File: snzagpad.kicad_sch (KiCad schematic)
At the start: 79 parts, among them J1 USB_C, J3 SWD, SW0 Boot, SW1 ?, SW10 ?, SW11 ?, SW12 ?, SW13 ?, SW14 ?, SW15 ?, SW16 ?, SW17 ?, SW18 ?, SW19 ?, SW2 ?, SW20 ?, SW21 ?, SW22 ?, SW23 ?, SW3 ?, SW4 ?, SW5 ?, SW6 ?, SW7 ?, SW8 ?, SW9 ?, U1 RP2040, U2 SRV05-4, U3 XC6206, U4 W25Q128JVS, Y1 12MHz

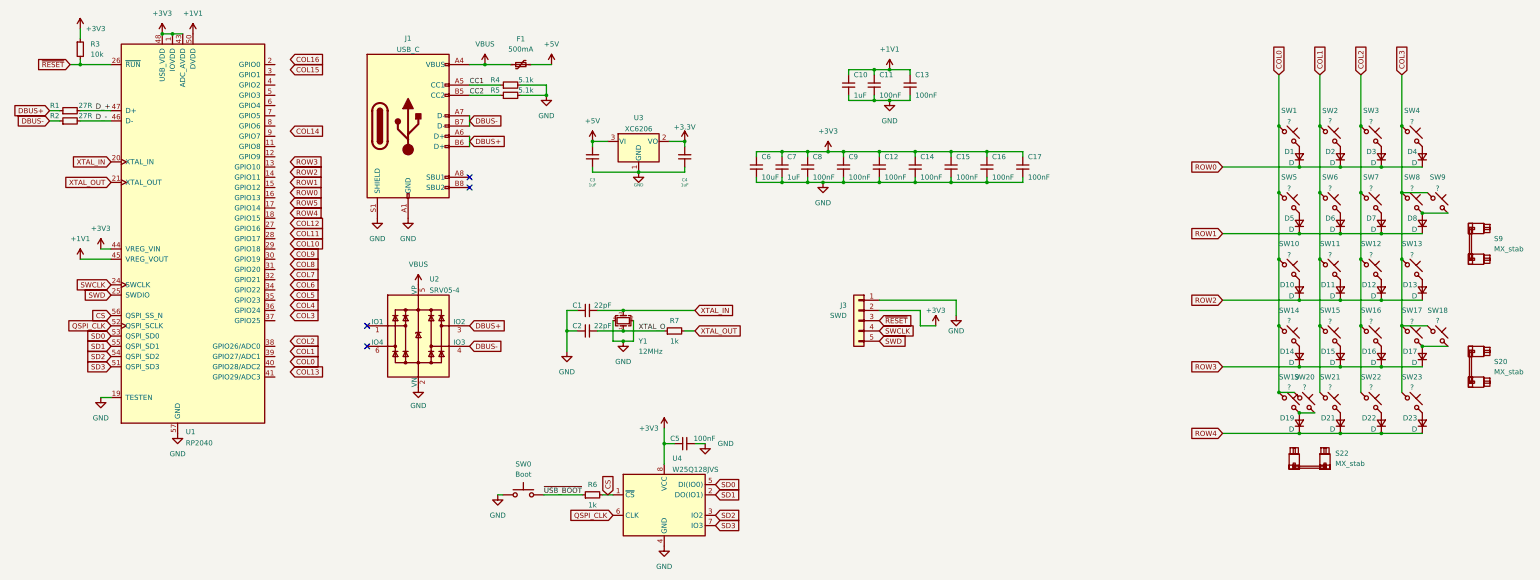
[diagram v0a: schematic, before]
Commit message: Updated outline, added mounts, preliminary routing
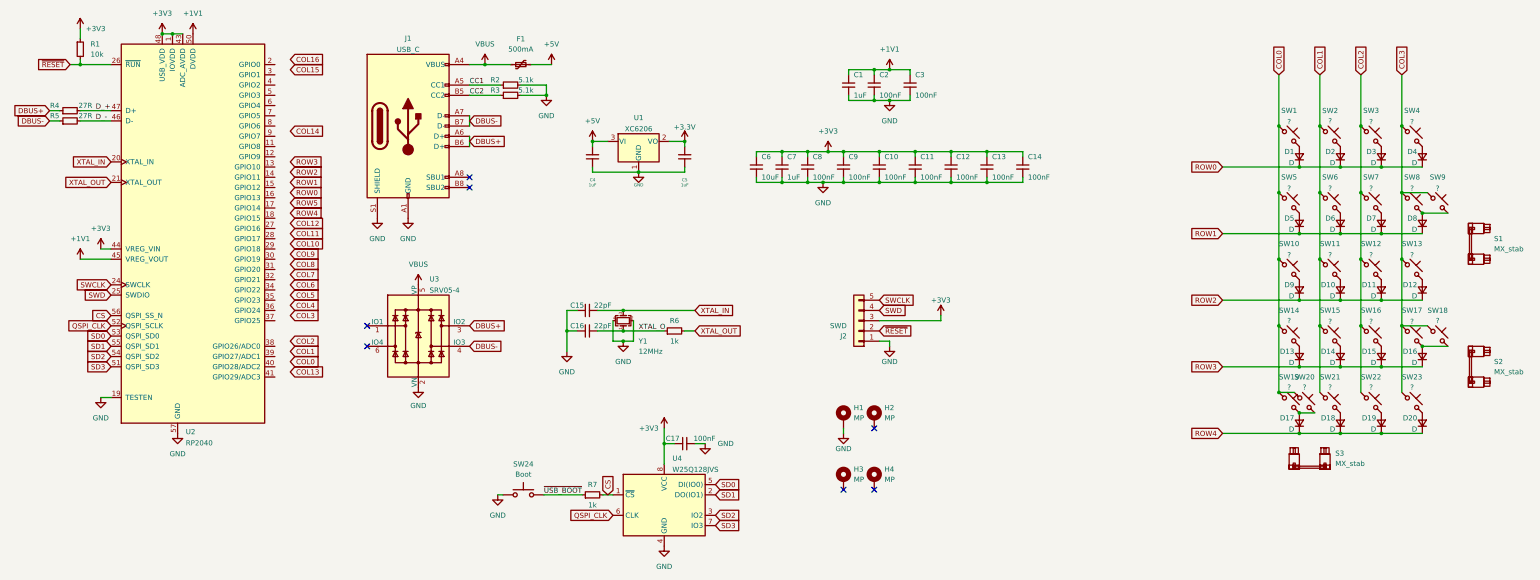
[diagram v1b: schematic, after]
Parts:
- added H1, H2, H3, H4: MP, MountingHole:MountingHole_2.2mm_M2_Pad, symbol Mechanical:MountingHole_Pad
- renumbered C10 to C1, C12 to C10, C14 to C11, C15 to C12, C16 to C13, C17 to C14, C1 to C15, C2 to C16, C5 to C17, C11 to C2, C13 to C3, C3 to C4, C4 to C5, D11 to D10, D12 to D11, D13 to D12, D14 to D13, D15 to D14, D16 to D15, D17 to D16, D19 to D17, D21 to D18, D22 to D19, D23 to D20, D10 to D9, J3 to J2, R3 to R1, R4 to R2, R5 to R3, R1 to R4, R2 to R5, R7 to R6, R6 to R7, S9 to S1, S20 to S2, S22 to S3, SW0 to SW24, U3 to U1, U1 to U2, U2 to U3
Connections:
- net +3V3: now also J2.3 (Pin_3); no longer J2.2 (Pin_2)
- net GND: now also H1.1
- net SWCLK: now also J2.5 (Pin_5); no longer J2.4 (Pin_4)
- net SWD: now also J2.4 (Pin_4); no longer J2.5 (Pin_5)
- net ~{RESET}: now also J2.2 (Pin_2); no longer J2.3 (Pin_3)
- no-connect marks 4 -> 7
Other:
- moved on the sheet: J2

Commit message: Edited cutout, mounts, USB position, routing
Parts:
- H1, H2, H3, H4: footprint MountingHole:MountingHole_2.2mm_M2_Pad -> MountingHole:MountingHole_2.2mm_M2_ISO14580_Pad
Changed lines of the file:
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@@
       (effects (font (size 1.27 1.27)) (justify left))
     )
-    (property "Footprint" "MountingHole:MountingHole_2.2mm_M2_Pad" (id 2) (at 234.95 134.62 0)
+    (property "Footprint" "MountingHole:MountingHole_2.2mm_M2_ISO14580_Pad" (id 2) (at 234.95 134.62 0)
       (effects (font (size 1.27 1.27)) hide)
     )
@@
       (effects (font (size 1.27 1.27)) (justify left))
     )
-    (property "Footprint" "MountingHole:MountingHole_2.2mm_M2_Pad" (id 2) (at 227.33 134.62 0)
+    (property "Footprint" "MountingHole:MountingHole_2.2mm_M2_ISO14580_Pad" (id 2) (at 227.33 134.62 0)
       (effects (font (size 1.27 1.27)) hide)
     )
@@
       (effects (font (size 1.27 1.27)) (justify left))
     )
-    (property "Footprint" "MountingHole:MountingHole_2.2mm_M2_Pad" (id 2) (at 227.33 119.38 0)
+    (property "Footprint" "MountingHole:MountingHole_2.2mm_M2_ISO14580_Pad" (id 2) (at 227.33 119.38 0)
       (effects (font (size 1.27 1.27)) hide)
     )
@@
       (effects (font (size 1.27 1.27)) (justify left))
     )
-    (property "Footprint" "MountingHole:MountingHole_2.2mm_M2_Pad" (id 2) (at 234.95 119.38 0)
+    (property "Footprint" "MountingHole:MountingHole_2.2mm_M2_ISO14580_Pad" (id 2) (at 234.95 119.38 0)
       (effects (font (size 1.27 1.27)) hide)
     )
@@
     )
     (path "/92ea1021-2dae-4d4a-b211-86ccee3ba4ed"
-      (reference "H1") (unit 1) (value "MP") (footprint "MountingHole:MountingHole_2.2mm_M2_Pad")
+      (reference "H1") (unit 1) (value "MP") (footprint "MountingHole:MountingHole_2.2mm_M2_ISO14580_Pad")
     )
     (path "/d755a3d1-521d-4d0c-aa97-92b99354f491"
-      (reference "H2") (unit 1) (value "MP") (footprint "MountingHole:MountingHole_2.2mm_M2_Pad")
+      (reference "H2") (unit 1) (value "MP") (footprint "MountingHole:MountingHole_2.2mm_M2_ISO14580_Pad")
     )
     (path "/5e972ae4-6f53-4eb5-97ac-b15ba7b7e923"
-      (reference "H3") (unit 1) (value "MP") (footprint "MountingHole:MountingHole_2.2mm_M2_Pad")
+      (reference "H3") (unit 1) (value "MP") (footprint "MountingHole:MountingHole_2.2mm_M2_ISO14580_Pad")
     )
     (path "/1aab2a5d-e09c-4385-855d-bfb45a77c796"
-      (reference "H4") (unit 1) (value "MP") (footprint "MountingHole:MountingHole_2.2mm_M2_Pad")
+      (reference "H4") (unit 1) (value "MP") (footprint "MountingHole:MountingHole_2.2mm_M2_ISO14580_Pad")
     )
     (path "/57dbda62-d28b-4d83-a763-2f2823178cf5"

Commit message: Completed mostly, rounded traces, connected everything
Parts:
- H1, H2, H3, H4, S1, S2, S3: now left out of the parts list
- J1: LCSC (none) -> C2982555
- SW1, SW10, SW11, SW12, SW13, SW14, SW15, SW16, SW17, SW18, SW19, SW2, SW20, SW21, SW22, SW23, SW3, SW4, SW5, SW6, SW7, SW8, SW9: LCSC (none) -> C2803348
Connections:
- net COL0: now also SW19.2, SW20.2, U2.8 (GPIO6); no longer SW19.1, SW20.1
- net COL1: now also U2.7 (GPIO5)
- net COL2: now also U2.6 (GPIO4)
- net COL3: now also U2.5 (GPIO3)
- net ROW0: now also U2.35 (GPIO23)
- net ROW1: now also U2.34 (GPIO22)
- net ROW2: now also U2.4 (GPIO2)
- net ROW3: now also U2.3 (GPIO1)
- net ROW4: now also U2.2 (GPIO0)
- new net: D17.2 (A), SW19.1, SW20.1
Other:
- moved on the sheet: SW19, SW20

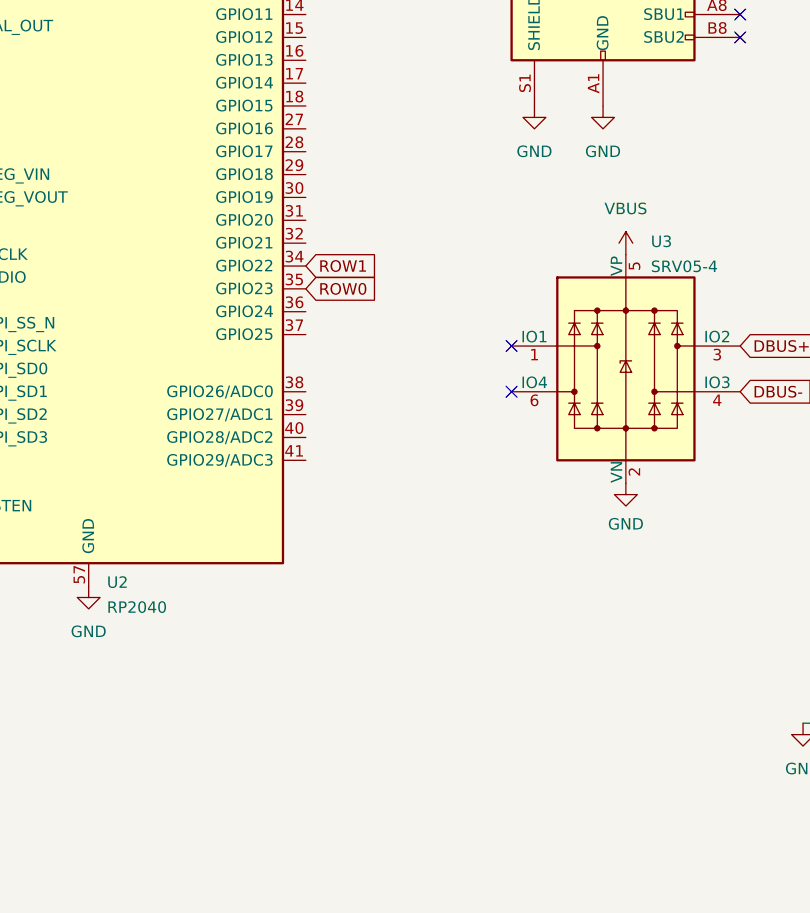
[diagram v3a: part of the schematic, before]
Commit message: Added GPIO breakout
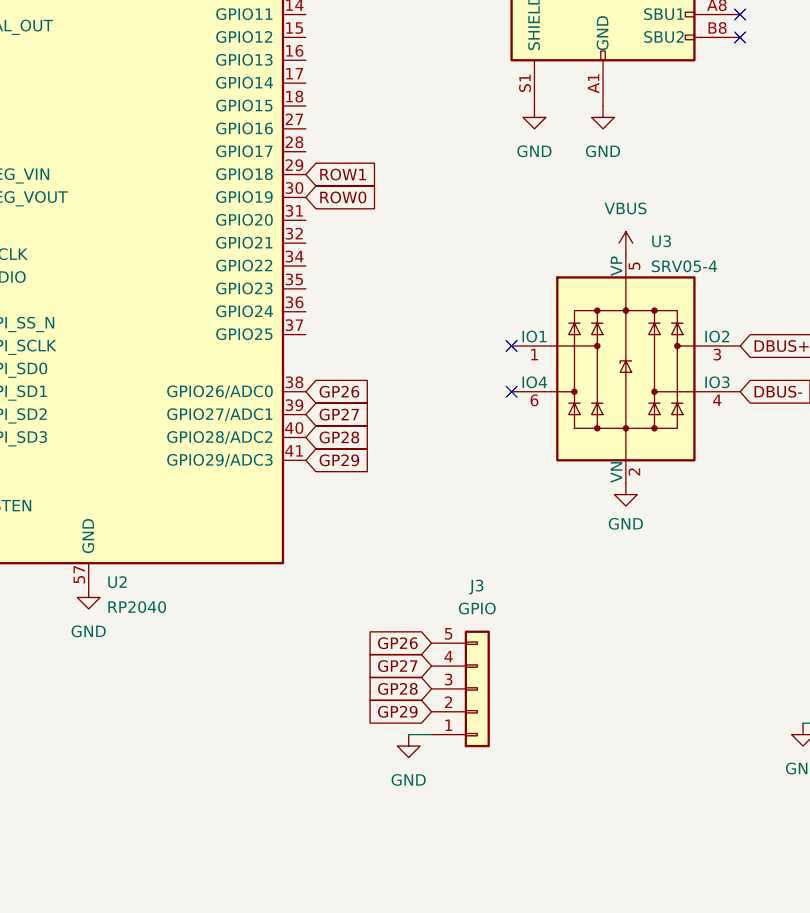
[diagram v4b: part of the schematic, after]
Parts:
- added J3: GPIO, Connector_PinHeader_1.00mm:PinHeader_1x05_P1.00mm_Vertical, symbol Connector_Generic:Conn_01x05
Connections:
- net GND: now also J3.1 (Pin_1)
- net ROW0: now also U2.30 (GPIO19); no longer U2.35 (GPIO23)
- net ROW1: now also U2.29 (GPIO18); no longer U2.34 (GPIO22)
- net GP26: now reaches U2.38 (GPIO26/ADC0)
- net GP26: now also J3.5 (Pin_5)
- net GP27: now reaches U2.39 (GPIO27/ADC1)
- net GP27: now also J3.4 (Pin_4)
- net GP28: now reaches U2.40 (GPIO28/ADC2)
- net GP28: now also J3.3 (Pin_3)
- net GP29: now reaches U2.41 (GPIO29/ADC3)
- net GP29: now also J3.2 (Pin_2)
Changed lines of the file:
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@@
+    (stroke (width 0) (type default) (color 0 0 0 0))
+  )
+  (wire (pts (xy 97.79 139.7) (xy 100.33 139.7))
     (stroke (width 0) (type default) (color 0 0 0 0))
   )
@@
     )
   )
-  (global_label "ROW1" (shape input) (at 86.36 87.63 0) (fields_autoplaced)
-    (effects (font (size 1.27 1.27)) (justify left))
-    (property "Intersheet References" "${INTERSHEET_REFS}" (id 0) (at 94.0345 87.5506 0)
+  (global_label "ROW1" (shape input) (at 86.36 77.47 0) (fields_autoplaced)
+    (effects (font (size 1.27 1.27)) (justify left))
+    (property "Intersheet References" "${INTERSHEET_REFS}" (id 0) (at 94.0345 77.3906 0)
       (effects (font (size 1.27 1.27)) (justify left) hide)
     )
@@
     )
   )
+  (global_label "GP28" (shape input) (at 100.33 134.62 180) (fields_autoplaced)
+    (effects (font (size 1.27 1.27)) (justify right))
+    (property "Intersheet References" "${INTERSHEET_REFS}" (id 0) (at 92.9579 134.5406 0)
+      (effects (font (size 1.27 1.27)) (justify right) hide)
+    )
+  )
   (global_label "COL0" (shape input) (at 335.28 34.29 90) (fields_autoplaced)
     (effects (font (size 1.27 1.27)) (justify left))
@@
     )
   )
-  (global_label "ROW0" (shape input) (at 86.36 90.17 0) (fields_autoplaced)
-    (effects (font (size 1.27 1.27)) (justify left))
-    (property "Intersheet References" "${INTERSHEET_REFS}" (id 0) (at 94.0345 90.0906 0)
+  (global_label "ROW0" (shape input) (at 86.36 80.01 0) (fields_autoplaced)
+    (effects (font (size 1.27 1.27)) (justify left))
+    (property "Intersheet References" "${INTERSHEET_REFS}" (id 0) (at 94.0345 79.9306 0)
       (effects (font (size 1.27 1.27)) (justify left) hide)
     )
@@
     (property "Intersheet References" "${INTERSHEET_REFS}" (id 0) (at 94.0345 34.2106 0)
       (effects (font (size 1.27 1.27)) (justify left) hide)
+    )
+  )
+  (global_label "GP27" (shape input) (at 100.33 132.08 180) (fields_autoplaced)
+    (effects (font (size 1.27 1.27)) (justify right))
+    (property "Intersheet References" "${INTERSHEET_REFS}" (id 0) (at 92.9579 132.0006 0)
+      (effects (font (size 1.27 1.27)) (justify right) hide)
     )
   )
@@
     )
   )
+  (global_label "GP26" (shape input) (at 86.36 101.6 0) (fields_autoplaced)
+    (effects (font (size 1.27 1.27)) (justify left))
+    (property "Intersheet References" "${INTERSHEET_REFS}" (id 0) (at 93.7321 101.5206 0)
+      (effects (font (size 1.27 1.27)) (justify left) hide)
+    )
+  )
   (global_label "SD2" (shape input) (at 45.72 104.14 180) (fields_autoplaced)
     (effects (font (size 1.27 1.27)) (justify right))
@@
     )
   )
+  (global_label "GP29" (shape input) (at 100.33 137.16 180) (fields_autoplaced)
+    (effects (font (size 1.27 1.27)) (justify right))
+    (property "Intersheet References" "${INTERSHEET_REFS}" (id 0) (at 92.9579 137.0806 0)
+      (effects (font (size 1.27 1.27)) (justify right) hide)
+    )
+  )
+  (global_label "GP29" (shape input) (at 86.36 109.22 0) (fields_autoplaced)
+    (effects (font (size 1.27 1.27)) (justify left))
+    (property "Intersheet References" "${INTERSHEET_REFS}" (id 0) (at 93.7321 109.1406 0)
+      (effects (font (size 1.27 1.27)) (justify left) hide)
+    )
+  )
   (global_label "DBUS-" (shape input) (at 134.62 101.6 0) (fields_autoplaced)
     (effects (font (size 1.27 1.27)) (justify left))
     (property "Intersheet References" "${INTERSHEET_REFS}" (id 0) (at 143.6855 101.5206 0)
+      (effects (font (size 1.27 1.27)) (justify left) hide)
+    )
+  )
+  (global_label "GP27" (shape input) (at 86.36 104.14 0) (fields_autoplaced)
+    (effects (font (size 1.27 1.27)) (justify left))
+    (property "Intersheet References" "${INTERSHEET_REFS}" (id 0) (at 93.7321 104.0606 0)
       (effects (font (size 1.27 1.27)) (justify left) hide)
     )
@@
     )
   )
+  (global_label "GP28" (shape input) (at 86.36 106.68 0) (fields_autoplaced)
+    (effects (font (size 1.27 1.27)) (justify left))
+    (property "Intersheet References" "${INTERSHEET_REFS}" (id 0) (at 93.7321 106.6006 0)
+      (effects (font (size 1.27 1.27)) (justify left) hide)
+    )
+  )
   (global_label "CS" (shape input) (at 45.72 93.98 180) (fields_autoplaced)
     (effects (font (size 1.27 1.27)) (justify right))
@@
     )
   )
+  (global_label "GP26" (shape input) (at 100.33 129.54 180) (fields_autoplaced)
+    (effects (font (size 1.27 1.27)) (justify right))
+    (property "Intersheet References" "${INTERSHEET_REFS}" (id 0) (at 92.9579 129.4606 0)
+      (effects (font (size 1.27 1.27)) (justify right) hide)
+    )
+  )
   (global_label "ROW4" (shape input) (at 321.31 123.19 180) (fields_autoplaced)
     (effects (font (size 1.27 1.27)) (justify right))
@@
   (symbol (lib_id "power:GND") (at 227.33 123.19 0) (mirror y) (unit 1)
     (in_bom yes) (on_board yes)
-    (property "Reference" "#PWR0101" (id 0) (at 227.33 129.54 0)
+    (property "Reference" "#PWR027" (id 0) (at 227.33 129.54 0)
       (effects (font (size 1.27 1.27)) hide)
     )
@@
   (symbol (lib_id "power:GND") (at 141.605 138.43 0) (unit 1)
     (in_bom yes) (on_board yes)
-    (property "Reference" "#PWR028" (id 0) (at 141.605 144.78 0)
+    (property "Reference" "#PWR029" (id 0) (at 141.605 144.78 0)
       (effects (font (size 1.27 1.27)) hide)
     )
@@
   (symbol (lib_id "power:GND") (at 193.04 125.73 0) (unit 1)
     (in_bom yes) (on_board yes)
-    (property "Reference" "#PWR027" (id 0) (at 193.04 132.08 0)
+    (property "Reference" "#PWR028" (id 0) (at 193.04 132.08 0)
       (effects (font (size 1.27 1.27)) hide)
     )
@@
     (pin "2")
   )
+  (symbol (lib_id "power:GND") (at 97.79 139.7 0) (unit 1)
+    (in_bom yes) (on_board yes) (fields_autoplaced)
+    (property "Reference" "#PWR030" (id 0) (at 97.79 146.05 0)
+      (effects (font (size 1.27 1.27)) hide)
+    )
+    (property "Value" "GND" (id 1) (at 97.79 144.78 0))
+    (property "Footprint" "" (id 2) (at 97.79 139.7 0)
+      (effects (font (size 1.27 1.27)) hide)
+    )
+    (property "Datasheet" "" (id 3) (at 97.79 139.7 0)
+      (effects (font (size 1.27 1.27)) hide)
+    )
+    (pin "1")
+  )
   (symbol (lib_id "marbastlib-mx:MX_SW_HS") (at 337.82 66.04 0) (unit 1)
     (in_bom yes) (on_board yes) (fields_autoplaced)
@@
   (symbol (lib_id "power:GND") (at 182.88 151.13 0) (unit 1)
     (in_bom yes) (on_board yes)
-    (property "Reference" "#PWR029" (id 0) (at 182.88 157.48 0)
+    (property "Reference" "#PWR031" (id 0) (at 182.88 157.48 0)
       (effects (font (size 1.27 1.27)) hide)
     )
@@
     )
     (pin "1")
+  )
+  (symbol (lib_id "Connector_Generic:Conn_01x05") (at 105.41 134.62 0) (mirror x) (unit 1)
+    (in_bom no) (on_board yes) (fields_autoplaced)
+    (property "Reference" "J3" (id 0) (at 105.41 123.19 0))
+    (property "Value" "GPIO" (id 1) (at 105.41 125.73 0))
+    (property "Footprint" "Connector_PinHeader_1.00mm:PinHeader_1x05_P1.00mm_Vertical" (id 2) (at 105.41 134.62 0)
+      (effects (font (size 1.27 1.27)) hide)
+    )
+    (property "Datasheet" "~" (id 3) (at 105.41 134.62 0)
+      (effects (font (size 1.27 1.27)) hide)
+    )
+    (pin "1")
+    (pin "2")
+    (pin "3")
+    (pin "4")
+    (pin "5")
   )
   (symbol (lib_id "Switch:SW_Push") (at 147.955 138.43 0) (unit 1)
@@
       (reference "#PWR026") (unit 1) (value "GND") (footprint "")
     )
+    (path "/2feaa8de-fe5b-49ef-9409-da9dfd6321d6"
+      (reference "#PWR027") (unit 1) (value "GND") (footprint "")
+    )
     (path "/5fc8739f-bef5-48db-9a89-1ea4cbdf6e61"
-      (reference "#PWR027") (unit 1) (value "GND") (footprint "")
+      (reference "#PWR028") (unit 1) (value "GND") (footprint "")
     )
     (path "/470e4f37-aa60-47d4-94b0-efb251f9f5c8"
-      (reference "#PWR028") (unit 1) (value "GND") (footprint "")
+      (reference "#PWR029") (unit 1) (value "GND") (footprint "")
+    )
+    (path "/6db9d57d-52dc-4240-9006-aa82065028c0"
+      (reference "#PWR030") (unit 1) (value "GND") (footprint "")
     )
     (path "/814e5de4-b99b-44f0-ab9f-c94cdc3961e9"
-      (reference "#PWR029") (unit 1) (value "GND") (footprint "")
-    )
-    (path "/2feaa8de-fe5b-49ef-9409-da9dfd6321d6"
-      (reference "#PWR0101") (unit 1) (value "GND") (footprint "")
+      (reference "#PWR031") (unit 1) (value "GND") (footprint "")
     )
     (path "/64f2da51-e688-441e-9cd7-6cbff6f89742"
@@
       (reference "J2") (unit 1) (value "SWD") (footprint "Connector_PinSocket_2.54mm:PinSocket_1x05_P2.54mm_Vertical")
     )
+    (path "/87777781-4579-4616-ad66-868dd67869eb"
+      (reference "J3") (unit 1) (value "GPIO") (footprint "Connector_PinHeader_1.00mm:PinHeader_1x05_P1.00mm_Vertical")
+    )
     (path "/46feb8ab-1398-4613-b39c-fa63c64fbc47"
